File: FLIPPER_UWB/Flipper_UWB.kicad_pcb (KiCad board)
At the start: 2 copper layers, 34 x 67 mm, 25 parts, among them IC1 DWM1000, J1 Conn_01x08_Socket, J2 Conn_01x10_Socket

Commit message: Update UWB
Update PCB UWB
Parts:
- removed kibuzzard-644981B9: G***, kibuzzard-644981B9
- removed kibuzzard-644981FD: G***, kibuzzard-644981FD
- removed kibuzzard-64498233: G***, kibuzzard-64498233
- removed kibuzzard-64498280: G***, kibuzzard-64498280
- removed kibuzzard-644982A0: G***, kibuzzard-644982A0
- removed kibuzzard-644982E2: G***, kibuzzard-644982E2
- removed kibuzzard-644982F5: G***, kibuzzard-644982F5
- added kibuzzard-644AA5E2: G***, kibuzzard-644AA5E2, F.Cu at (150.9, 82.8)
- added kibuzzard-644AA5EC: G***, kibuzzard-644AA5EC, F.Cu at (150.9, 87.8)
- added kibuzzard-644AA5FA: G***, kibuzzard-644AA5FA, F.Cu at (150.9, 110.6)
- added kibuzzard-644AA606: G***, kibuzzard-644AA606, F.Cu at (151.3, 113.3)
- added kibuzzard-644AA610: G***, kibuzzard-644AA610, F.Cu at (150.9, 115.8)
- added kibuzzard-644AA622: G***, kibuzzard-644AA622, F.Cu at (150.5, 120.8)
- added kibuzzard-644AA62C: G***, kibuzzard-644AA62C, F.Cu at (150.5, 123.4)
- moved G*** 0.40 mm to (151.1, 108.0), turned to 180 degrees
- moved G*** 0.30 mm to (151.1, 90.4), turned to 180 degrees
- moved G*** 0.20 mm to (151.1, 85.3), turned to 180 degrees
- moved G*** 0.10 mm to (151.0, 67.5), turned to 180 degrees

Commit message: Update PCB shield UWB
Update PCB shield UWB
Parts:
- moved kibuzzard-644AA606 5.30 mm to (151.2, 118.6)
- moved G*** 1.92 mm to (132.3, 119.6)
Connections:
- J1 pad 3: /CS -> unconnected-(J1-Pin_3-Pad3)
- J1 pad 5: unconnected-(J1-Pin_5-Pad5) -> /CS
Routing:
- net +3.3V: track 114.6 -> 41.9 mm, vias 0 -> 1
- net /CS: track 70.4 -> 67.1 mm
- net /RSTN: track 124.7 -> 124.1 mm

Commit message: Update shield UWB
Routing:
- net +3.3V: track 41.9 -> 44.2 mm
- net /LED3: track 19.6 -> 20.8 mm
- net /LED4: track 24.7 -> 25.7 mm
- net /LED2: track 15.0 -> 15.9 mm
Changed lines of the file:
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@@
   (segment (start 128.924 81.9345) (end 128.924 83.3345) (width 0.5) (layer "F.Cu") (net 5))
   (via (at 136.2 83.9) (size 0.8) (drill 0.4) (layers "F.Cu" "B.Cu") (net 5))
-  (segment (start 136.2 83.9) (end 136.3 84) (width 0.5) (layer "B.Cu") (net 5))
-  (segment (start 136.3 84) (end 144.8 84) (width 0.5) (layer "B.Cu") (net 5))
-  (segment (start 144.8 84) (end 151.1732 90.3732) (width 0.5) (layer "B.Cu") (net 5))
-  (segment (start 151.1732 90.3732) (end 153.8732 90.3732) (width 0.5) (layer "B.Cu") (net 5))
+  (segment (start 153.8732 90.3732) (end 148.3732 90.3732) (width 0.5) (layer "B.Cu") (net 5))
+  (segment (start 145.9 84) (end 136.3 84) (width 0.5) (layer "B.Cu") (net 5))
+  (segment (start 148.3732 90.3732) (end 146.9 88.9) (width 0.5) (layer "B.Cu") (net 5))
+  (segment (start 146.9 85) (end 145.9 84) (width 0.5) (layer "B.Cu") (net 5))
+  (segment (start 136.3 84) (end 136.2 83.9) (width 0.5) (layer "B.Cu") (net 5))
+  (segment (start 146.9 88.9) (end 146.9 85) (width 0.5) (layer "B.Cu") (net 5))
   (segment (start 129.567 96.935) (end 129.5545 96.9225) (width 0.25) (layer "F.Cu") (net 6))
   (segment (start 140.824 74.4357) (end 140.824 75.8357) (width 0.25) (layer "F.Cu") (net 6))
@@
   (segment (start 148.0655 77.7345) (end 148.1345 77.7345) (width 0.25) (layer "F.Cu") (net 18))
   (segment (start 148.1345 77.7345) (end 148.3 77.9) (width 0.25) (layer "F.Cu") (net 18))
-  (segment (start 134.524 95.792) (end 134.524 87.0295) (width 0.25) (layer "F.Cu") (net 20))
+  (segment (start 134.524 94.524) (end 134.524 87.0295) (width 0.25) (layer "F.Cu") (net 20))
+  (segment (start 135.667 96.935) (end 135.667 95.667) (width 0.25) (layer "F.Cu") (net 20))
   (segment (start 135.667 96.935) (end 136.0045 96.5975) (width 0.25) (layer "F.Cu") (net 20))
-  (segment (start 135.667 96.935) (end 134.524 95.792) (width 0.25) (layer "F.Cu") (net 20))
-  (segment (start 136.5045 89.085) (end 135.924 88.5045) (width 0.25) (layer "F.Cu") (net 21))
-  (segment (start 135.924 88.5045) (end 135.924 87.0295) (width 0.25) (layer "F.Cu") (net 21))
-  (segment (start 136.5045 100.5975) (end 136.5045 89.085) (width 0.25) (layer "F.Cu") (net 21))
-  (segment (start 135.667 101.435) (end 136.5045 100.5975) (width 0.25) (layer "F.Cu") (net 21))
-  (segment (start 137.324 104.278) (end 135.667 105.935) (width 0.25) (layer "F.Cu") (net 22))
-  (segment (start 137.324 87.0295) (end 137.324 104.278) (width 0.25) (layer "F.Cu") (net 22))
-  (segment (start 138.724 107.378) (end 138.724 87.0295) (width 0.25) (layer "F.Cu") (net 23))
-  (segment (start 135.667 110.435) (end 138.724 107.378) (width 0.25) (layer "F.Cu") (net 23))
+  (segment (start 135.667 95.667) (end 134.524 94.524) (width 0.25) (layer "F.Cu") (net 20))
+  (segment (start 136.565 101.435) (end 137 101) (width 0.25) (layer "F.Cu") (net 21))
+  (segment (start 135.667 101.435) (end 136.565 101.435) (width 0.25) (layer "F.Cu") (net 21))
+  (segment (start 137 89.9) (end 135.924 88.824) (width 0.25) (layer "F.Cu") (net 21))
+  (segment (start 135.924 88.824) (end 135.924 87.0295) (width 0.25) (layer "F.Cu") (net 21))
+  (segment (start 137 101) (end 137 89.9) (width 0.25) (layer "F.Cu") (net 21))
+  (segment (start 137.899 87.6045) (end 137.899 88.5785) (width 0.25) (layer "F.Cu") (net 22))
+  (segment (start 137.899 88.5785) (end 137.9 88.5795) (width 0.25) (layer "F.Cu") (net 22))
+  (segment (start 137.9 104.9) (end 136.865 105.935) (width 0.25) (layer "F.Cu") (net 22))
+  (segment (start 136.865 105.935) (end 135.667 105.935) (width 0.25) (layer "F.Cu") (net 22))
+  (segment (start 137.324 87.0295) (end 137.899 87.6045) (width 0.25) (layer "F.Cu") (net 22))
+  (segment (start 137.9 88.5795) (end 137.9 104.9) (width 0.25) (layer "F.Cu") (net 22))
+  (segment (start 137.365 110.435) (end 138.724 109.076) (width 0.25) (layer "F.Cu") (net 23))
+  (segment (start 135.667 110.435) (end 137.365 110.435) (width 0.25) (layer "F.Cu") (net 23))
+  (segment (start 138.724 109.076) (end 138.724 87.0295) (width 0.25) (layer "F.Cu") (net 23))
   (zone (net 6) (net_name "GND") (layer "F.Cu") (hatch edge 0.5)
     (connect_pads (clearance 0.5))

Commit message: Add_HTML
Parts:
- removed the G*** at (151.1, 108.0)
- removed the G*** at (151.1, 90.4)
- removed the G*** at (151.0, 67.5)
- removed the G*** at (151.1, 85.3)
- moved G*** 0.27 mm to (132.5, 119.7)
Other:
- board text added: "Flipper Zero UWB Shield"
- board text removed: "FlipperZero UWB Shield"

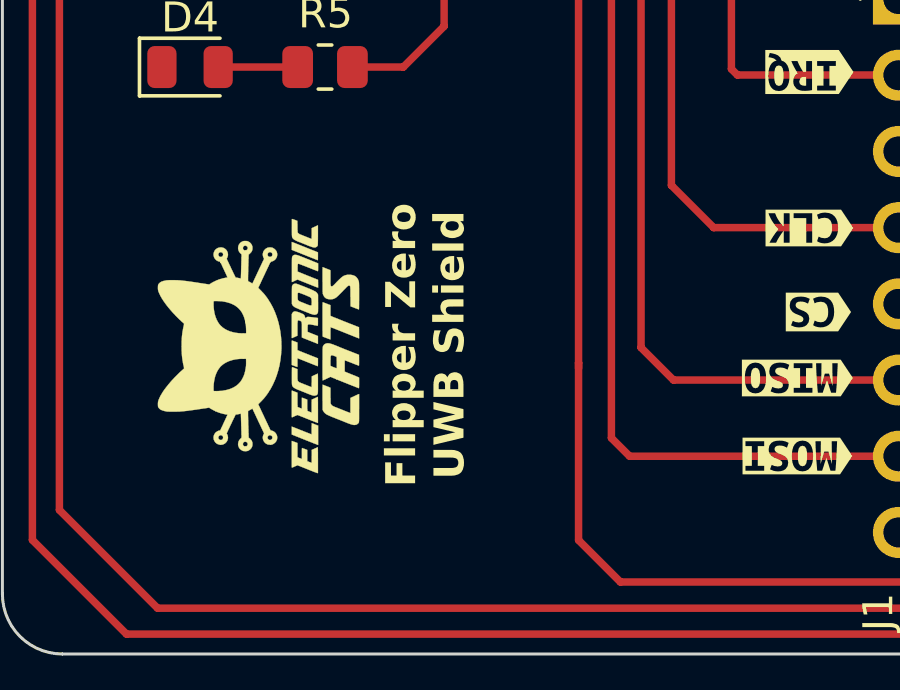
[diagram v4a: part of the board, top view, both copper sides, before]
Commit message: feat: rename addons
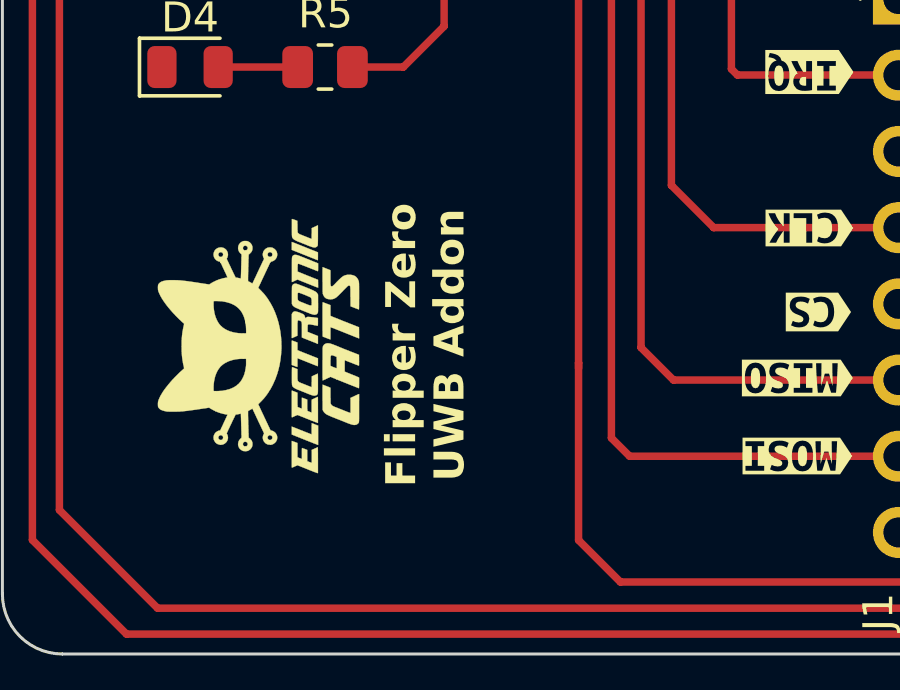
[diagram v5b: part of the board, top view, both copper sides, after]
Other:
- board text added: "Flipper Zero UWB Addon"
- board text removed: "Flipper Zero UWB Shield"
